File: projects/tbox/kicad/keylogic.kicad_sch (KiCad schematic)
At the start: 63 parts, among them Q2101 2N7002, Q2102 2N7002, Q2103 2N7002, Q2104 2N7002, Q2105 2N7002, Q2106 2N7002, Q2107 2N7002, SW2101 PTT A, SW2102 PTT B, SW2103 OVERRIDE, SW2104 MUTE A, SW2105 MUTE B

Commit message: Review fixes, mechanical: footprints, switch codes, PTC and LED resistors
- TY-250P footprint: stray ')' truncated the body/courtyard/silk; fixed
  (transformers now have a courtyard on the board).
- SJ-43514: tip pad at +3.6 from the axis, pin-5 hole at +1.6 (3.2 from
  pin 3) per a closer reading of the SJ-4351X drawing.
- C&K 7101 AV2 and 7201/7203 V-bracket: terminal holes 1.85 mm (0.073 in)
  per catalog pages F-11/F-13; DPDT terminal columns 0.190 in apart and
  bracket legs 0.250 in apart (they were swapped).
- Switch functions: PVA OA is momentary and EE is push-push, so PTT/
  intercom get OA and the mutes EE; override toggle 7201 (on-none-on)
  -> 7203 (on-off-on).
- PTC MPN 1812L050/60MR; TX LED resistor 680R -> 2k2 and all seven LED
  resistors to 0805.
Board footprints refreshed in place; the resulting courtyard overlaps are
resolved by the placement fixes that follow.
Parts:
- R2102: value 680R -> 2k2; footprint Resistor_SMD:R_0603_1608Metric -> Resistor_SMD:R_0805_2012Metric
- R2106, R2110, R2114, R2119, R2120: footprint Resistor_SMD:R_0603_1608Metric -> Resistor_SMD:R_0805_2012Metric
- SW2101, SW2102: MPN PVA1EEH2xxxxxxV2 (momentary; height at layout) -> PVA1OAH2xxxxxxV2 (OA = momentary; height code at layout)
- SW2103: MPN 7201MD9V6BE -> 7203MD9V6BE
- SW2104, SW2105: MPN PVA1OAH2xxxxxxV2 (latching; height at layout) -> PVA1EEH2xxxxxxV2 (EE = push-push latching; height code at l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
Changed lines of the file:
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@@
 			)
 		)
-		(property "MPN" "PVA1OAH2xxxxxxV2 (latching; height at layout)"
+		(property "MPN" "PVA1EEH2xxxxxxV2 (EE = push-push latching; height code at layout)"
 			(at 133.35 118.11 0)
 			(hide yes)
@@
 			)
 		)
-		(property "Footprint" "Resistor_SMD:R_0603_1608Metric"
+		(property "Footprint" "Resistor_SMD:R_0805_2012Metric"
 			(at 119.38 152.4 0)
 			(hide yes)
@@
 			)
 		)
-		(property "MPN" "PVA1OAH2xxxxxxV2 (latching; height at layout)"
+		(property "MPN" "PVA1EEH2xxxxxxV2 (EE = push-push latching; height code at layout)"
 			(at 133.35 133.35 0)
 			(hide yes)
@@
 			)
 		)
-		(property "MPN" "7201MD9V6BE"
+		(property "MPN" "7203MD9V6BE"
 			(at 128.27 81.28 0)
 			(hide yes)
@@
 			)
 		)
-		(property "Footprint" "Resistor_SMD:R_0603_1608Metric"
+		(property "Footprint" "Resistor_SMD:R_0805_2012Metric"
 			(at 144.78 152.4 0)
 			(hide yes)
@@
 			)
 		)
-		(property "Value" "680R"
+		(property "Value" "2k2"
 			(at 45.72 153.67 0)
 			(show_name no)
@@
 			)
 		)
-		(property "Footprint" "Resistor_SMD:R_0603_1608Metric"
+		(property "Footprint" "Resistor_SMD:R_0805_2012Metric"
 			(at 43.18 152.4 0)
 			(hide yes)
@@
 			)
 		)
-		(property "MPN" "PVA1EEH2xxxxxxV2 (momentary; height at layout)"
+		(property "MPN" "PVA1OAH2xxxxxxV2 (OA = momentary; height code at layout)"
 			(at 35.56 127 0)
 			(hide yes)
@@
 			)
 		)
-		(property "MPN" "7201MD9V6BE"
+		(property "MPN" "7203MD9V6BE"
 			(at 128.27 96.52 0)
 			(hide yes)
@@
 			)
 		)
-		(property "Footprint" "Resistor_SMD:R_0603_1608Metric"
+		(property "Footprint" "Resistor_SMD:R_0805_2012Metric"
 			(at 68.58 152.4 0)
 			(hide yes)
@@
 			)
 		)
-		(property "Footprint" "Resistor_SMD:R_0603_1608Metric"
+		(property "Footprint" "Resistor_SMD:R_0805_2012Metric"
 			(at 93.98 152.4 0)
 			(hide yes)
@@
 			)
 		)
-		(property "MPN" "PVA1EEH2xxxxxxV2 (momentary; height at layout)"
+		(property "MPN" "PVA1OAH2xxxxxxV2 (OA = momentary; height code at layout)"
 			(at 35.56 86.36 0)
 			(hide yes)
@@
 			)
 		)
-		(property "Footprint" "Resistor_SMD:R_0603_1608Metric"
+		(property "Footprint" "Resistor_SMD:R_0805_2012Metric"
 			(at 167.64 152.4 0)
 			(hide yes)

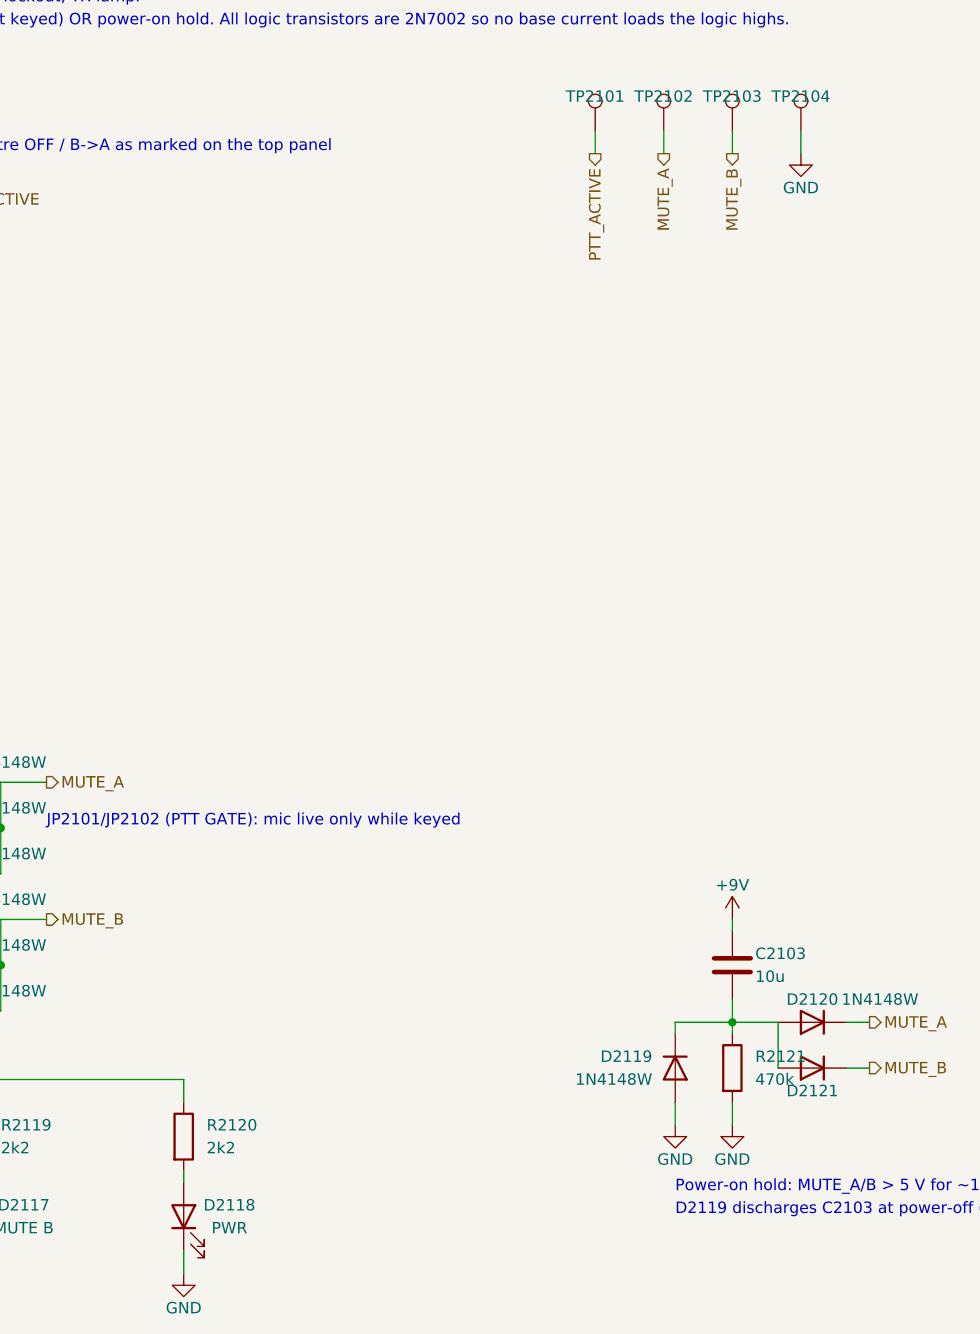
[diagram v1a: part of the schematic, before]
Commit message: Review design changes: chassis returns, OPA1622 phones amps, RX-in protection, supervisor, mute fade, gains, BLEND buffer, jack-side protection, mic-jack bias
Decisions Q1-Q9 from the 2026-09-08 adversarial review:
- Q1 (D): phones jack sleeves and TRRS ring 2 on CHASSIS; GND-CHASSIS
  ties per board (NT1001 front at the headset jacks, NT2401 control at
  the phones amps, NT3201 rear) with chassis studs H1001/H2401; phones
  return rides the chassis, never the ribbon ground.
- Q2 (B'): U2401/U2403 NJM4556A -> OPA1622 (new tbox symbol, VSON-10),
  build-out 10R -> 3R3, EN from PWR_OK.
- Q3 (A+C): RX-in coupling caps non-polar 10u, 2k2 series, 1N4148W
  clamps to the rails at the op-amp inputs (SMAJ15CA stays at the jack).
- Q4 (B): TPS3808G01 supervisor on +9 V (7.5 V, ~1.2 s) -> PWR_OK;
  MUTE_HOLD inverter replaces the RC hold, shunts PTT_ACTIVE; Q3201 gets
  a 100k gate pull-down.
- Q5 (A): mute fades (2k2 + back-to-back 2N7002 shunt to Vref, ~5 ms)
  before the TS12A12511 switches (~30 ms, immediate release).
- Q6 (A): preamp LO +28 / HI +40 dB (R1104 430R, R1106 3k3).
- Q7 (A): BLEND is an inverting summer on U3301B (R3318 22k, C3317).
- Q8 (C): phones RF filters move to the front board at the jacks; SP724
  arrays on every front jack contact and the rear PTT inputs; SMAJ15CA
  across each isolated line-out secondary.
- Q9 (B'): 3.5 mm mic jack tip carries the mic, tip and ring both get
  2k2 bias (R1109/C1109).
DESIGN.md, LEVELS.md and TODO.md updated; ERC 0, check_sch/boards/
footprints/power clean; power tree regenerated.
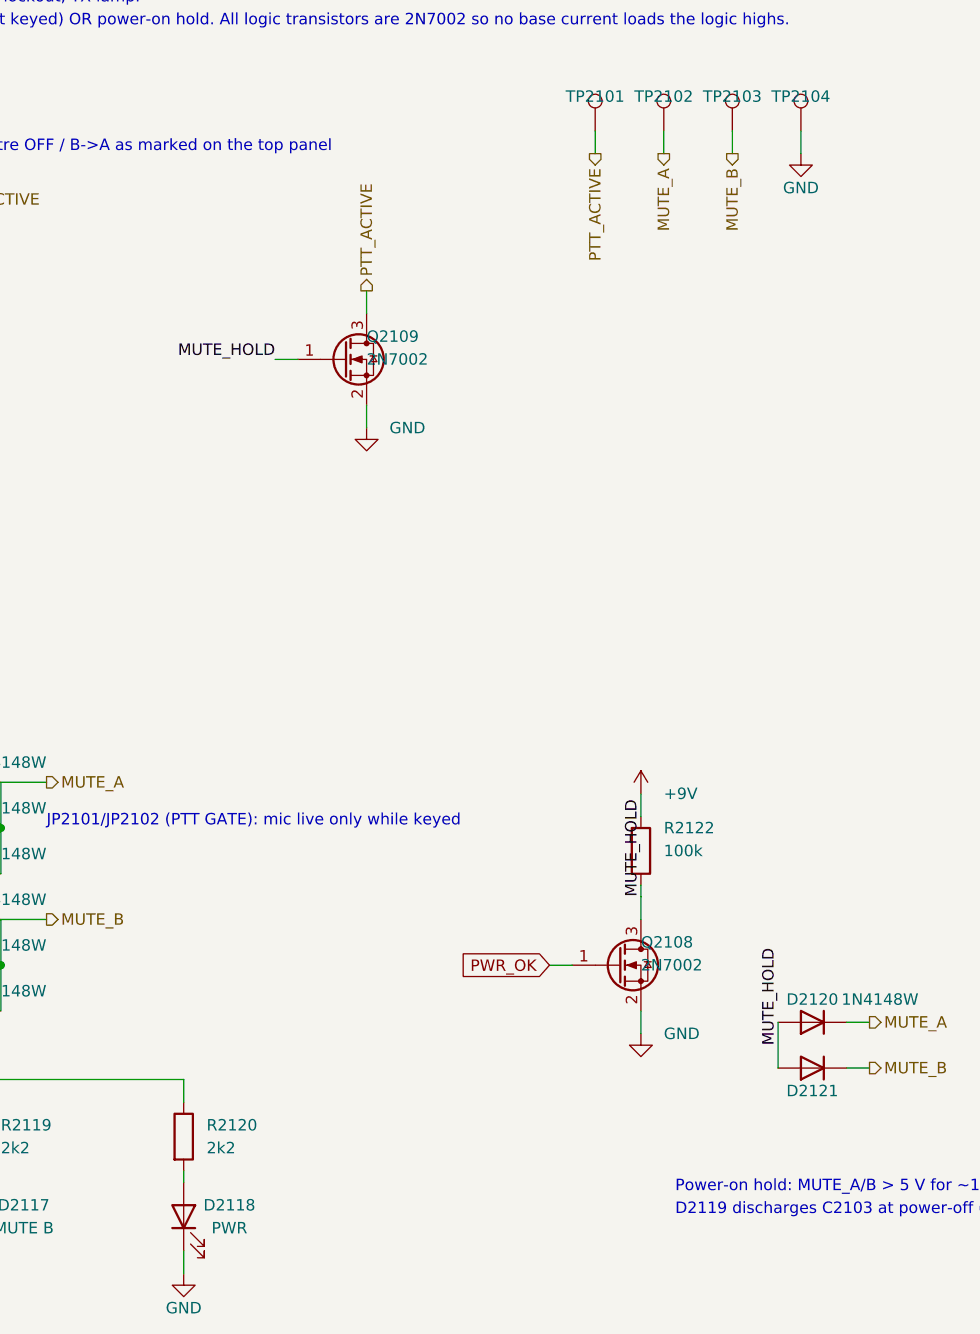
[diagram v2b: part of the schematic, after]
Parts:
- removed C2103: 10u, Capacitor_SMD:C_1206_3216Metric, symbol Device:C
- removed D2119: 1N4148W, Diode_SMD:D_SOD-123, symbol tbox:1N4148W
- removed R2121: 470k, Resistor_SMD:R_0603_1608Metric, symbol Device:R
- added Q2108, Q2109: 2N7002, Package_TO_SOT_SMD:SOT-23, symbol tbox:2N7002
- added R2122: 100k, Resistor_SMD:R_0603_1608Metric, symbol Device:R
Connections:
- net +9V: now also R2122.1
- net GND: now also Q2108.2 (S), Q2109.2 (S)
- net PTT_ACTIVE: now also Q2109.3 (D)
- net MUTE_HOLD: now reaches D2120.2 (A), D2121.2 (A)
- net MUTE_HOLD: now also Q2108.3 (D), Q2109.1 (G), R2122.2
- new net PWR_OK: Q2108.1 (G)

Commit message: Datasheet README: OPA1622, TPS3808, SP724
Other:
- note added: "Power-on / brown-out hold: PWR_OK (TPS3808, Supply sheet) low -> Q2108 raises MUTE_HOLD:"
- note added: "both mutes on through D2120/D2121, PTT_ACTIVE shunted by Q2109, phones amps disabled."
- note removed: "D2119 discharges C2103 at power-off (quick re-arm)."
- note removed: "Power-on hold: MUTE_A/B > 5 V for ~1 s (C2103/R2121, 1M loads);"
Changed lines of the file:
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@@
 		)
 	)
-	(text "D2119 discharges C2103 at power-off (quick re-arm)."
+	(text "both mutes on through D2120/D2121, PTT_ACTIVE shunted by Q2109, phones amps disabled."
 		(exclude_from_sim no)
 		(at 222.25 161.29 0)
@@
 		)
 	)
-	(text "Power-on hold: MUTE_A/B > 5 V for ~1 s (C2103/R2121, 1M loads);"
+	(text "Power-on / brown-out hold: PWR_OK (TPS3808, Supply sheet) low -> Q2108 raises MUTE_HOLD:"
 		(exclude_from_sim no)
 		(at 222.25 158.75 0)
@@
 		)
 	)
-	(label "MUTE_HOLD"
-		(at 218.44 125.73 90)
-		(effects
-			(font
-				(size 1.27 1.27)
-			)
-			(justify left bottom)
-		)
-	)
 	(symbol
 		(lib_id "Device:R")
@@
 		)
 	)
+	(label "MUTE_HOLD"
+		(at 218.44 126.37 0)
+		(effects
+			(font
+				(size 1.27 1.27)
+			)
+			(justify left bottom)
+		)
+	)

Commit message: Review 2: load maxima and the resistor rule
- Op-amp maxima from the datasheets: OPA1678 duals 4/6 (5.6 mA IQ over
  temperature), line drivers 4/10, OPA1622 6/101 (8.4 mA IQ + two
  145 mA-peak class-B channels).
- Every resistor with an end on a rail now needs Load_mA (Vref returns
  and the ADP7142 output RC exempt): R2122, R2501, R2505, R2507,
  R3209/R3210 (1k gain-select pull-ups, 9 mA each when closed),
  R3201/R3202 PTT pull-ups annotated.
- Load_mA syntax is strict (n or n/m).
- RAW_13V8 capability 400 mA (1812L050 hold at 50 C), not 500.
- C3401/C3402 10u X7R 25V, GRM31CR71E106KA12L.
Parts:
- R2122: Load_mA (none) -> 0.09
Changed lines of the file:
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@@
+			)
+		)
+		(property "Load_mA" "0.09"
+			(at 218.44 120.65 0)
+			(show_name no)
+			(do_not_autoplace no)
+			(hide yes)
+			(effects
+				(font
+					(size 1.27 1.27)
+				)
 			)
 		)

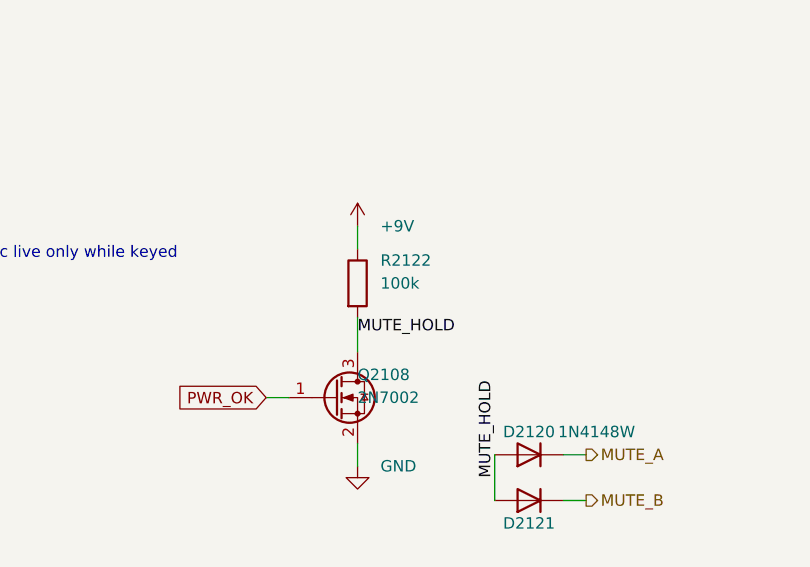
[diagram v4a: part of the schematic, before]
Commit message: Mute cell rework and a stronger supervisor pull-up (review 3, findings 4-6)
The mute command is now buffered once before it drives anything with a
capacitor on it, and both timing networks hang off that buffer:

- Q1203 (BSS138BK, Vgs(th) 0.48-1.6 V) inverts MUTE to MUTE_N; Q1204
  inverts that to MUTE_DRV, a stiff 0/+9 V copy with a 2k2 pull-up.
  Nothing can feed back into the diode-OR command line, which was what
  held MUTE at SW_CTL/2 and delayed reconnection by 101-285 ms.
- Fade gate: 4k7 + D1201 charge, 100k discharge returned to MUTE_DRV,
  470n. Both ends sit at +9 V when muted, so the gate reaches the full
  rail (4.5 V above Vref) instead of 7.0 V through the old 47k/470k
  divider and diode drop.
- Switch delay: 470k into 1u, with D1202 + 220R across it to dump the
  cap into Q1204 on release (about 1 ms at 35 mA) while the shunt still
  conducts. The 470k is chosen so even the earliest possible logic trip
  (0.8 V, the only bound the TS12A12511 gives at this supply) finds the
  shunt already conducting.
- Shunt pair is PMV30UN2, whose R_DS(on) is specified at 1.5 V of gate
  drive (100 mohm max, 43 mohm at 2.5 V): -60.8 dB against the 220R at
  brown-out drive, -70.7 dB at a healthy rail. The 2N7002 it replaces is
  specified only at 5 V and 10 V.
- R2122 100k -> 10k. Against the two channels' 100k command pull-downs
  it puts MUTE_HOLD at 7.0 V with the rail at 9 V and 4.5 V at 6 V,
  where 100k gave 2.8 V and 1.8 V against a threshold specified as high
  as 2.5 V. With the timing capacitors now behind each cell's buffer the
  key inhibit follows PWR_OK promptly instead of waiting for them.

Datasheets for both new parts added. Board synced and re-placed.
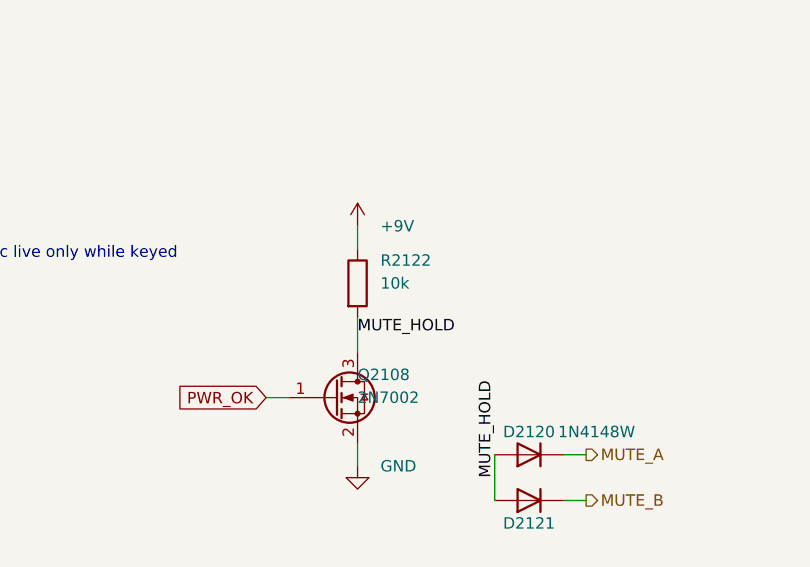
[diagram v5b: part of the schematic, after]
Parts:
- R2122: value 100k -> 10k; Load_mA 0.09 -> 0.9
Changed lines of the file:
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@@
 			)
 		)
-		(property "Value" "100k"
+		(property "Value" "10k"
 			(at 220.98 120.65 0)
 			(show_name no)
@@
 			)
 		)
-		(property "Load_mA" "0.09"
+		(property "Load_mA" "0.9"
 			(at 218.44 120.65 0)
 			(show_name no)
